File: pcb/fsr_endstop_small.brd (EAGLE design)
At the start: 27.9 x 30.5 mm, 33 parts, among them U1 ATTINY461

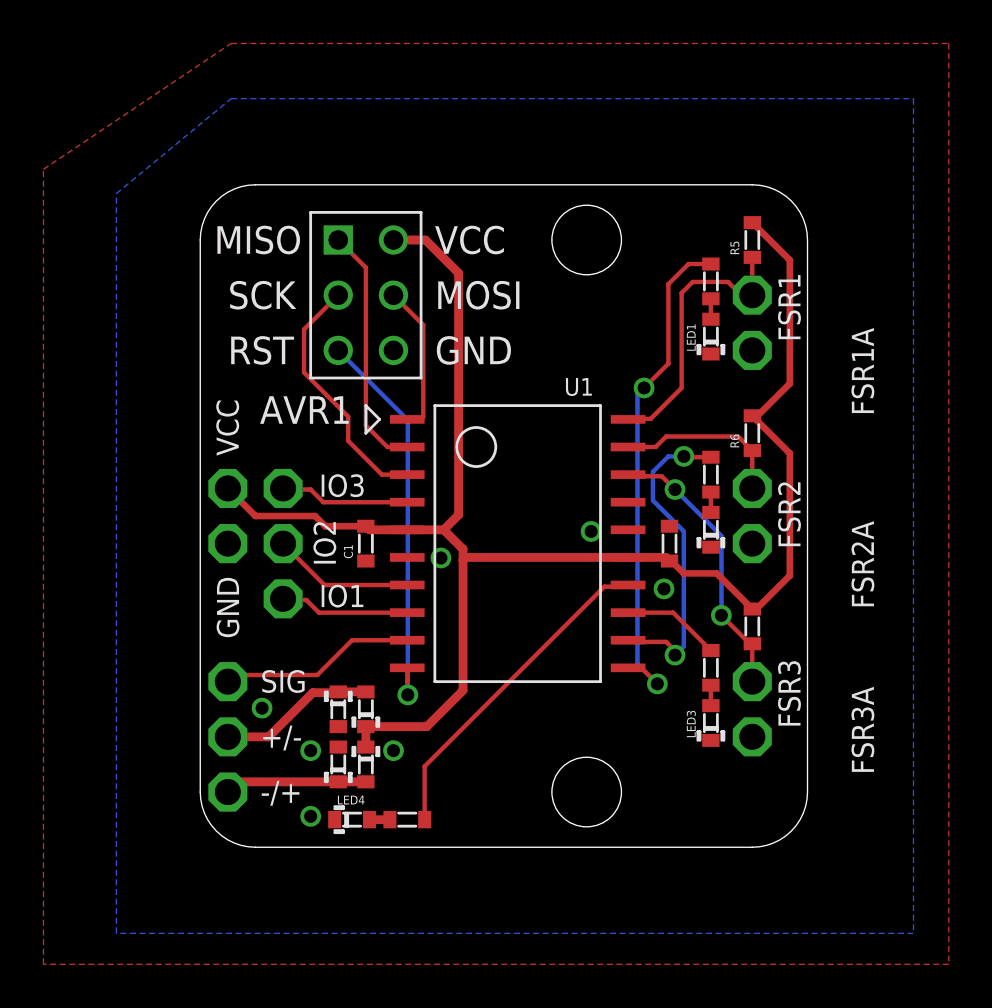
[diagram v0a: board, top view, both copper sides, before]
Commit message: Replaced the discrete diodes with a bridge rectifier chip for easier hand soldering.
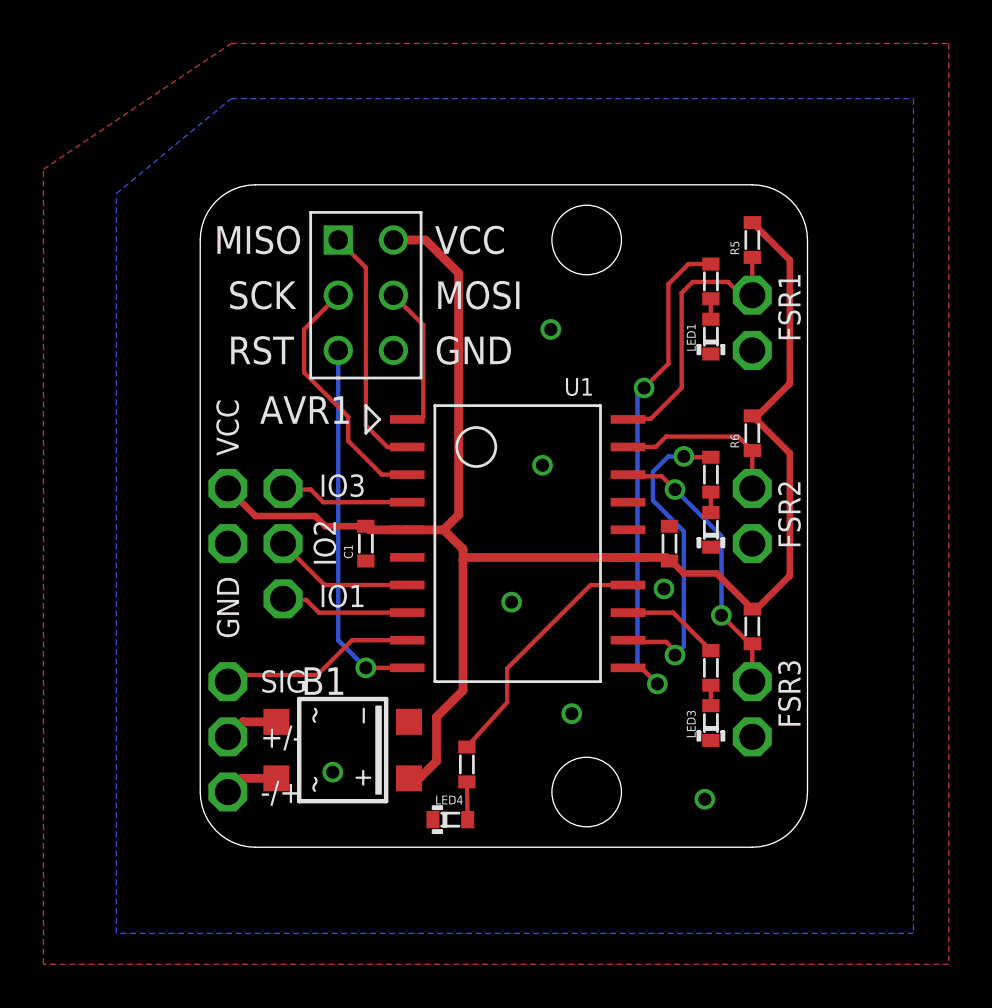
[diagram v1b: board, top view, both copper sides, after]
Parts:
- removed D1, D2, D3, D4: (no value), _sg_lib:0603_DIODE
- added B1: MB6S, rectifier:SOIC-4
- moved LED4 4.52 mm to (24.2, 14.0)
- moved R4 3.74 mm to (25.0, 16.5), turned to 270 degrees
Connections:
- net GND: now also B1.-; no longer D3.+, D4.+
- net N$3: now also B1.~2; no longer D2.+, D3.-
- net N$4: now also B1.~1; no longer D1.+, D4.-
- net V+: now also B1.+; no longer D1.-, D2.-
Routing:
- net N$4: track 7.23 -> 2.52 mm
- net N$3: track 6.54 -> 2.49 mm
- net N$10: track 15.3 -> 11.5 mm
- net N$6: track 18.4 -> 17.0 mm
- net N$21: track 0.94 -> 1.74 mm
- net V+: track 75.5 -> 74.8 mm
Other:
- board text added: "rev1.1"
- board text removed: "rev1"

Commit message: Made various fixes to the 1.1 version.
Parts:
- added U$1: (no value), SparkFun-Aesthetics:OSHW-LOGO-M
- moved B1 1.12 mm to (20.4, 17.2)
- moved LED4 0.91 mm to (25.1, 14.0)
- moved R4 0.91 mm to (25.9, 16.5)
- moved -/+ 0.72 mm to (14.1, 16.0)
- moved +/- 0.72 mm to (14.1, 18.5)
- moved SIG 0.72 mm to (14.1, 21.0)
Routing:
- net N$3: track 2.49 -> 3.28 mm
- net N$4: track 2.52 -> 3.25 mm
- net V+: track 74.8 -> 74.1 mm
- net N$10: track 11.5 -> 11.0 mm
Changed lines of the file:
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@@
 <hole x="30.48" y="15.24" drill="3.2"/>
 <hole x="30.48" y="40.64" drill="3.2"/>
-<text x="26.2128" y="17.78" size="2.1844" layer="22" font="vector" rot="MR90">FSR Endstop</text>
-<text x="22.86" y="17.78" size="2.1844" layer="22" font="vector" rot="MR90">Controller</text>
-<text x="19.05" y="17.78" size="2.1844" layer="22" font="vector" rot="MR90">rev1.1</text>
+<text x="25.8064" y="17.78" size="2.1844" layer="22" font="vector" rot="MR90">FSR Endstop</text>
+<text x="21.844" y="17.78" size="2.1844" layer="22" font="vector" rot="MR90">Controller</text>
+<text x="18.1356" y="17.78" size="2.1844" layer="22" font="vector" rot="MR90">rev1.1</text>
 </plain>
 <attributes>
@@
 <attribute name="NAME" x="29.4386" y="33.4772" size="0.8128" layer="21" font="vector"/>
 </element>
-<element name="SIG" library="_sg_lib" package="PIN_1.2MM" value="PIN1.2MM" x="13.97" y="20.32"/>
-<element name="+/-" library="_sg_lib" package="PIN_1.2MM" value="PIN1.2MM" x="13.97" y="17.78"/>
-<element name="-/+" library="_sg_lib" package="PIN_1.2MM" value="PIN1.2MM" x="13.97" y="15.24"/>
+<element name="SIG" library="_sg_lib" package="PIN_1.2MM" value="PIN1.2MM" x="14.0716" y="21.0312" smashed="yes">
+<attribute name="NAME" x="15.1652" y="19.6168" size="1.016" layer="21" font="vector"/>
+</element>
+<element name="+/-" library="_sg_lib" package="PIN_1.2MM" value="PIN1.2MM" x="14.0716" y="18.4912" smashed="yes">
+<attribute name="NAME" x="14.6572" y="16.8736" size="1.016" layer="21" font="vector"/>
+</element>
+<element name="-/+" library="_sg_lib" package="PIN_1.2MM" value="PIN1.2MM" x="14.0716" y="15.9512" smashed="yes">
+<attribute name="NAME" x="14.3524" y="14.1304" size="1.016" layer="21" font="vector"/>
+</element>
 <element name="FSR1" library="_sg_lib" package="PIN_1.2MM" value="PIN1.2MM" x="38.1" y="38.1" smashed="yes" rot="R180">
 <attribute name="NAME" x="39.3018" y="39.14" size="1.016" layer="21" font="vector" rot="R270"/>
@@
 </element>
 <element name="FSR3A" library="_sg_lib" package="PIN_1.2MM" value="PIN1.2MM" x="38.1" y="17.78" smashed="yes" rot="R180"/>
-<element name="AVR1" library="_sg_misc" package="AVR6" value="AVR6" x="20.32" y="38.1" smashed="yes">
-<attribute name="NAME" x="15.4432" y="32.1818" size="1.27" layer="25" font="vector"/>
-</element>
+<element name="AVR1" library="_sg_misc" package="AVR6" value="AVR6" x="20.32" y="38.1" smashed="yes"/>
 <element name="C1" library="_sg_lib" package="0603" value="1uF" x="20.32" y="26.67" rot="R90"/>
 <element name="LED1" library="_sg_lib" package="0603_DIODE" value="LED0603" x="36.195" y="36.195" rot="R90"/>
@@
 </element>
 <element name="LED3" library="_sg_lib" package="0603_DIODE" value="LED0603" x="36.195" y="18.415" rot="R90"/>
-<element name="LED4" library="_sg_lib" package="0603_DIODE" value="LED0603" x="24.2062" y="13.97"/>
+<element name="LED4" library="_sg_lib" package="0603_DIODE" value="LED0603" x="25.1206" y="13.97"/>
 <element name="R1" library="_sg_lib" package="0603" value="" x="36.195" y="38.735" smashed="yes" rot="R270">
 <attribute name="NAME" x="35.0678" y="39.3334" size="0.4064" layer="25" font="vector" rot="R270"/>
@@
 <attribute name="VALUE" x="35.895" y="21.755" size="0.3048" layer="51" font="vector" rot="R270"/>
 </element>
-<element name="R4" library="_sg_lib" package="0603" value="" x="24.9682" y="16.51" smashed="yes" rot="R270">
-<attribute name="NAME" x="23.841" y="16.8036" size="0.4064" layer="25" font="vector" rot="R270"/>
-<attribute name="NAME" x="25.0682" y="17.31" size="0.3048" layer="51" font="vector" rot="R270"/>
-<attribute name="VALUE" x="24.6682" y="17.31" size="0.3048" layer="51" font="vector" rot="R270"/>
+<element name="R4" library="_sg_lib" package="0603" value="" x="25.8826" y="16.51" smashed="yes" rot="R270">
+<attribute name="NAME" x="24.7554" y="16.8036" size="0.4064" layer="25" font="vector" rot="R270"/>
+<attribute name="NAME" x="25.9826" y="17.31" size="0.3048" layer="51" font="vector" rot="R270"/>
+<attribute name="VALUE" x="25.5826" y="17.31" size="0.3048" layer="51" font="vector" rot="R270"/>
 </element>
 <element name="R5" library="_sg_lib" package="0603" value="10k" x="38.1" y="40.64" rot="R90"/>
@@
 </element>
 <element name="IO1" library="_sg_lib" package="PIN_1.2MM" value="PIN1.2MM" x="16.51" y="24.13" smashed="yes">
-<attribute name="NAME" x="20.32" y="24.765" size="1.016" layer="21" font="vector" rot="R180"/>
+<attribute name="NAME" x="18.796" y="22.8346" size="1.016" layer="21" font="vector" rot="R180"/>
 </element>
 <element name="IO2" library="_sg_lib" package="PIN_1.2MM" value="PIN1.2MM" x="16.51" y="26.67" smashed="yes">
@@
 </element>
 <element name="IO3" library="_sg_lib" package="PIN_1.2MM" value="PIN1.2MM" x="16.51" y="29.21" smashed="yes">
-<attribute name="NAME" x="20.32" y="29.845" size="1.016" layer="21" font="vector" rot="R180"/>
+<attribute name="NAME" x="18.796" y="31.5722" size="1.016" layer="21" font="vector" rot="R180"/>
 </element>
 <element name="GND" library="_sg_lib" package="PIN_1.2MM" value="PIN1.2MM" x="13.97" y="26.67" rot="R270"/>
@@
 <attribute name="VALUE" x="33.99" y="27.47" size="0.3048" layer="51" font="vector" rot="R270"/>
 </element>
-<element name="B1" library="rectifier" package="SOIC-4" value="MB6S" x="19.2532" y="17.1704" rot="R270"/>
+<element name="B1" library="rectifier" package="SOIC-4" value="MB6S" x="20.3708" y="17.1704" smashed="yes" rot="R270">
+<attribute name="NAME" x="19.685" y="13.6144" size="0.8128" layer="25" font="vector"/>
+</element>
+<element name="U$1" library="SparkFun-Aesthetics" package="OSHW-LOGO-M" value="" x="31.1912" y="27.0256" rot="MR90"/>
 </elements>
 <signals>
@@
 <contactref element="-/+" pad="P$1"/>
 <contactref element="B1" pad="~2"/>
-<wire x1="13.97" y1="15.24" x2="14.6004" y2="15.8704" width="0.4064" layer="1"/>
-<wire x1="14.6004" y1="15.8704" x2="16.2032" y2="15.8704" width="0.4064" layer="1"/>
+<wire x1="14.0716" y1="15.9512" x2="17.24" y2="15.9512" width="0.4064" layer="1"/>
+<wire x1="17.24" y1="15.9512" x2="17.3208" y2="15.8704" width="0.4064" layer="1"/>
 </signal>
 <signal name="N$4">
 <contactref element="+/-" pad="P$1"/>
 <contactref element="B1" pad="~1"/>
-<wire x1="13.97" y1="17.78" x2="14.6604" y2="18.4704" width="0.4064" layer="1"/>
-<wire x1="14.6604" y1="18.4704" x2="16.2032" y2="18.4704" width="0.4064" layer="1"/>
+<wire x1="17.3208" y1="18.4704" x2="14.0716" y2="18.4912" width="0.4064" layer="1"/>
 </signal>
 <signal name="V+">
@@
 <contactref element="VCC" pad="P$1"/>
 <contactref element="C2" pad="2"/>
-<wire x1="24.7904" y1="19.9136" x2="24.7904" y2="25.908" width="0.4064" layer="1"/>
+<wire x1="24.7904" y1="17.0896" x2="24.7904" y2="25.908" width="0.4064" layer="1"/>
 <wire x1="24.7904" y1="25.908" x2="24.7904" y2="26.416" width="0.4064" layer="1"/>
 <wire x1="24.7904" y1="26.416" x2="23.9014" y2="27.305" width="0.4064" layer="1"/>
@@
 <wire x1="39.8272" y1="39.7128" x2="38.1" y2="41.44" width="0.3048" layer="1"/>
 <contactref element="B1" pad="+"/>
-<wire x1="22.3032" y1="15.8704" x2="22.7792" y2="15.8704" width="0.4064" layer="1"/>
-<wire x1="22.7792" y1="15.8704" x2="23.5712" y2="16.6624" width="0.4064" layer="1"/>
-<wire x1="23.5712" y1="16.6624" x2="23.5712" y2="18.6944" width="0.4064" layer="1"/>
-<wire x1="23.5712" y1="18.6944" x2="24.7904" y2="19.9136" width="0.4064" layer="1"/>
+<wire x1="23.4208" y1="15.8704" x2="23.5712" y2="15.8704" width="0.4064" layer="1"/>
+<wire x1="23.5712" y1="15.8704" x2="24.7904" y2="17.0896" width="0.4064" layer="1"/>
 </signal>
 <signal name="GND">
@@
 <via x="27.0256" y="23.9776" extent="1-16" drill="0.6"/>
 <via x="28.448" y="30.2768" extent="1-16" drill="0.6"/>
-<via x="18.796" y="16.1544" extent="1-16" drill="0.6"/>
+<via x="18.8976" y="16.3576" extent="1-16" drill="0.6"/>
 <via x="34.036" y="24.5872" extent="1-16" drill="0.6"/>
 <via x="28.829" y="36.5252" extent="1-16" drill="0.6"/>
@@
 <wire x1="30.6578" y1="24.765" x2="26.8224" y2="20.9296" width="0.2032" layer="1"/>
 <wire x1="26.8224" y1="20.9296" x2="26.8224" y2="19.3674" width="0.2032" layer="1"/>
-<wire x1="26.8224" y1="19.3674" x2="24.9682" y2="17.31" width="0.2032" layer="1"/>
+<wire x1="26.8224" y1="19.3674" x2="25.8826" y2="17.31" width="0.2032" layer="1"/>
 </signal>
 <signal name="N$11">
@@
 <contactref element="U1" pad="P$9"/>
 <wire x1="22.225" y1="22.225" x2="19.685" y2="22.225" width="0.2032" layer="1"/>
-<wire x1="19.685" y1="22.225" x2="18.0848" y2="20.6248" width="0.2032" layer="1"/>
-<wire x1="18.0848" y1="20.6248" x2="14.2748" y2="20.6248" width="0.2032" layer="1"/>
-<wire x1="14.2748" y1="20.6248" x2="13.97" y2="20.32" width="0.2032" layer="1"/>
+<wire x1="14.0716" y1="21.0312" x2="18.4912" y2="21.0312" width="0.2032" layer="1"/>
+<wire x1="18.4912" y1="21.0312" x2="19.685" y2="22.225" width="0.2032" layer="1"/>
 </signal>
 <signal name="N$16">
@@
 <contactref element="R4" pad="2"/>
 <contactref element="LED4" pad="+"/>
-<wire x1="25.0062" y1="13.97" x2="24.9682" y2="15.71" width="0.2032" layer="1"/>
+<wire x1="25.9206" y1="13.97" x2="25.8826" y2="15.71" width="0.2032" layer="1"/>
 </signal>
 <signal name="N$15">
